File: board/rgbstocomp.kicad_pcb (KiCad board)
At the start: 2 copper layers, 54 x 45 mm, 55 parts, among them U1 THS7316, U2 THS7316, U3 Opamp_Dual, U4 GS8743, U5 XC6206PxxxMR, Y1 TestPoint

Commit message: Fix CSYNC detection threashold
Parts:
- R27: value 1k -> 5k49
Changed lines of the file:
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@@
 			)
 		)
-		(property "Value" "1k"
+		(property "Value" "5k49"
 			(at 0 1.65 0)
 			(layer "F.Fab")

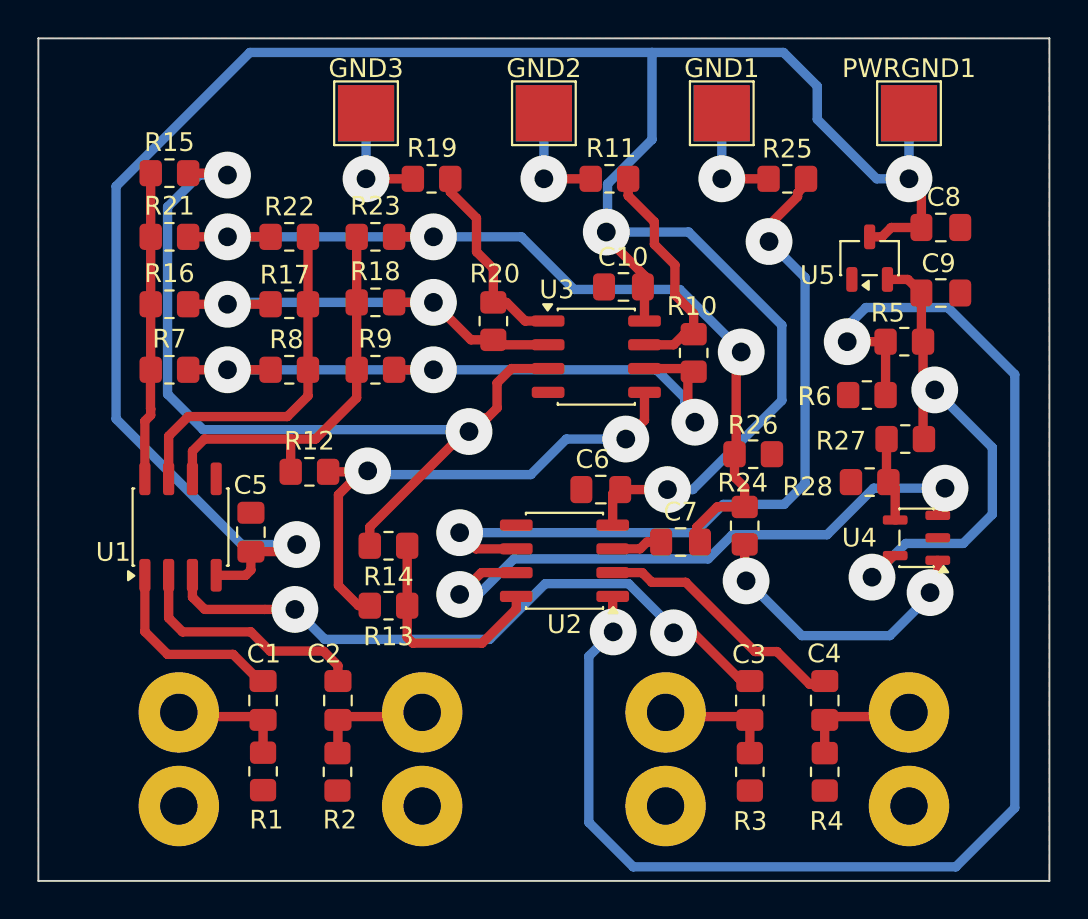
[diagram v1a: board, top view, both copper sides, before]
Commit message: Supply ICs with 3.3V instead of with 5V. Add documentation.
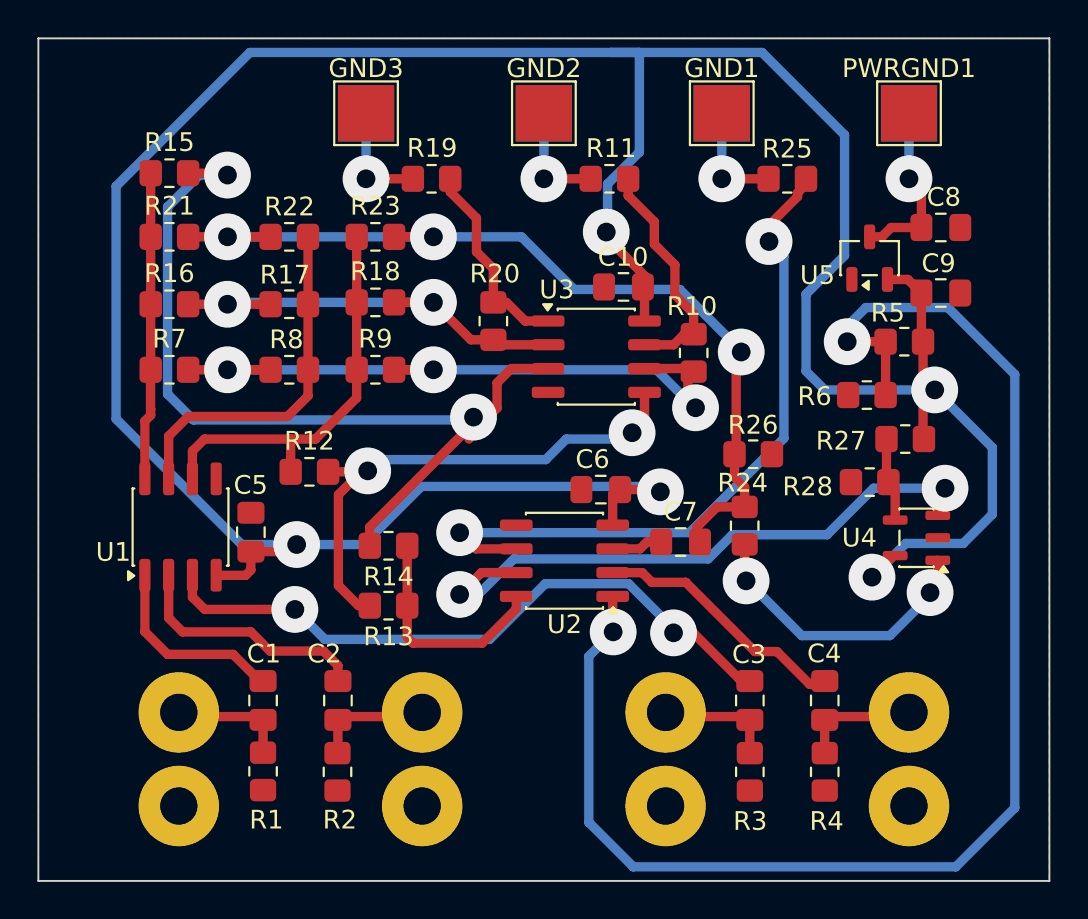
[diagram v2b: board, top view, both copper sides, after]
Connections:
- C10 pad 2: +5V -> +3V3
- C5 pad 2: +5V -> +3V3
- C6 pad 2: +5V -> +3V3
- U1 pad 4: +5V -> +3V3
- U2 pad 4: +5V -> +3V3
- U3 pad 8: +5V -> +3V3
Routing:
- net +3V3: track 29.2 -> 166.7 mm, vias 2 -> 5
- net +5V: track 133.4 -> 9.34 mm, vias 4 -> 1
- net Net-(U2-OUT3): track 40.8 -> 37.8 mm
- net Net-(U3A-+): track 48.3 -> 50.6 mm
- net Net-(U3B--): track 38.7 -> 37.3 mm
